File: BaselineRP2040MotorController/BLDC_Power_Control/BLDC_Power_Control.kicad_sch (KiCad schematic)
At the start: 7 parts, among them J3 Conn_01x03

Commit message: Change Mosfet Footprint.
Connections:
- net Motor Phase ${PhaseDesignator}/${PhaseDesignator}_OUT is gone; now on net Motor Phase ${PhaseDesignator}/${PhaseDesignator}_OUT: J3.3 (Pin_3)
- net Motor Phase ${PhaseDesignator}/${PhaseDesignator}_OUT: no longer J3.1 (Pin_1)
- new net Motor Phase ${PhaseDesignator}/${PhaseDesignator}_OUT: J3.1 (Pin_1)
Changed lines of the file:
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@@
 			(effects
 				(font
-					(size 0.001 0.001)
+					(size 0.0254 0.0254)
 				)
 				(hide yes)
@@
 			(effects
 				(font
-					(size 0.001 0.001)
+					(size 0.0254 0.0254)
 				)
 				(hide yes)
@@
 			(effects
 				(font
-					(size 0.001 0.001)
+					(size 0.0254 0.0254)
 				)
 				(hide yes)
@@
 			(effects
 				(font
-					(size 0.001 0.001)
+					(size 0.0254 0.0254)
 				)
 				(hide yes)
@@
 			(effects
 				(font
-					(size 0.001 0.001)
+					(size 0.0254 0.0254)
 				)
 				(hide yes)
@@
 			(effects
 				(font
-					(size 0.001 0.001)
+					(size 0.0254 0.0254)
 				)
 				(hide yes)
@@
 			(effects
 				(font
-					(size 0.001 0.001)
+					(size 0.0254 0.0254)
 				)
 				(hide yes)
@@
 			(effects
 				(font
-					(size 0.001 0.001)
+					(size 0.0254 0.0254)
 				)
 				(hide yes)
@@
 			(effects
 				(font
-					(size 0.001 0.001)
+					(size 0.0254 0.0254)
 				)
 				(hide yes)
@@
 			(effects
 				(font
-					(size 0.001 0.001)
-				)
-				(hide yes)
+					(size 0.0254 0.0254)
+				)
+				(hide yes)

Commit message: Drop some features.
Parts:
- C36, C37: footprint Capacitor_THT:CP_Radial_D10.0mm_P5.00mm -> Capacitor_SMD:CP_Elec_8x10
- J3: footprint parts:MT60-F.G.Y -> [EastMakes] Connectors:MT60-F.G.Y
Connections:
- net Motor Phase ${PhaseDesignator}/${PhaseDesignator}_OUT is gone; now on net Motor Phase ${PhaseDesignator}/${PhaseDesignator}_OUT: J3.3 (Pin_3)
- net Motor Phase ${PhaseDesignator}/${PhaseDesignator}_OUT: no longer J3.1 (Pin_1)
- new net Motor Phase ${PhaseDesignator}/${PhaseDesignator}_OUT: J3.1 (Pin_1)
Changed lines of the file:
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@@
 			)
 		)
-		(property "Footprint" "Capacitor_THT:CP_Radial_D10.0mm_P5.00mm"
+		(property "Footprint" "Capacitor_SMD:CP_Elec_8x10"
 			(at 249.8852 148.59 0)
 			(effects
@@
 			)
 		)
-		(property "Footprint" "Capacitor_THT:CP_Radial_D10.0mm_P5.00mm"
+		(property "Footprint" "Capacitor_SMD:CP_Elec_8x10"
 			(at 260.0452 148.59 0)
 			(effects
@@
 			)
 		)
-		(property "Footprint" "parts:MT60-F.G.Y"
+		(property "Footprint" "[EastMakes] Connectors:MT60-F.G.Y"
 			(at 170.18 74.93 0)
 			(effects

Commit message: Just before dropping the self build of the 2040
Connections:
- net Motor Phase ${PhaseDesignator}/${PhaseDesignator}_OUT is gone; now on net Motor Phase ${PhaseDesignator}/${PhaseDesignator}_OUT: J3.3 (Pin_3)
- net Motor Phase ${PhaseDesignator}/${PhaseDesignator}_OUT: no longer J3.1 (Pin_1)
- new net Motor Phase ${PhaseDesignator}/${PhaseDesignator}_OUT: J3.1 (Pin_1)
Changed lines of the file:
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@@
-	(wire
-		(pts
-			(xy 96.52 106.68) (xy 106.68 106.68)
-		)
-		(stroke
-			(width 0)
-			(type default)
-		)
-	)
 	(wire
 		(pts
@@
 		(fields_autoplaced yes)
 		(effects
-			(font
-				(size 1.27 1.27)
-				(bold yes)
-			)
-			(justify right)
-		)
-	)
-	(hierarchical_label "X_SENSE"
-		(shape output)
-		(at 96.52 106.68 180)
-		(fields_autoplaced yes)
-		(effects

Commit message: Release for Review
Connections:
- net Motor Phase ${PhaseDesignator}/${PhaseDesignator}_OUT is gone; now on net Motor Phase ${PhaseDesignator}/${PhaseDesignator}_OUT: J3.3 (Pin_3)
- net Motor Phase ${PhaseDesignator}/${PhaseDesignator}_OUT: no longer J3.1 (Pin_1)
- new net Motor Phase ${PhaseDesignator}/${PhaseDesignator}_OUT: J3.1 (Pin_1)
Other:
- moved on the sheet: C34, C35, C36, C37, C38, D14, J3

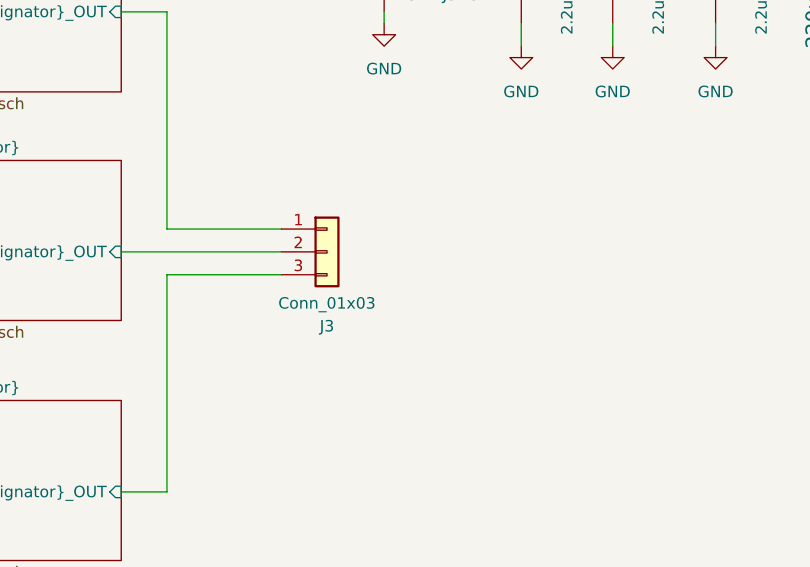
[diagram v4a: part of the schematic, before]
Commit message: Generate PDF
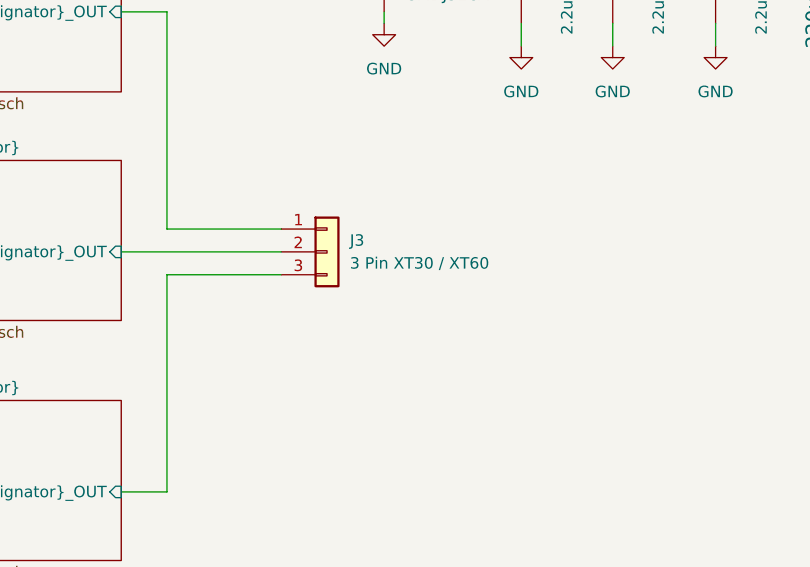
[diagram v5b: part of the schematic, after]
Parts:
- J3: value Conn_01x03 -> 3 Pin XT30 / XT60
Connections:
- net Motor Phase ${PhaseDesignator}/${PhaseDesignator}_OUT is gone; now on net Motor Phase ${PhaseDesignator}/${PhaseDesignator}_OUT: J3.3 (Pin_3)
- net Motor Phase ${PhaseDesignator}/${PhaseDesignator}_OUT: no longer J3.1 (Pin_1)
- new net Motor Phase ${PhaseDesignator}/${PhaseDesignator}_OUT: J3.1 (Pin_1)
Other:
- title: (none) -> BLDC Starting Point
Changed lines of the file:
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@@
 	(generator_version "8.0")
 	(paper "A5")
+	(title_block
+		(title "BLDC Starting Point")
+		(comment 1 "Florian, Josh and EMF Group Release")
+	)
 	(junction
 		(at 177.8 21.59)
@@
 		(fields_autoplaced yes)
 		(property "Reference" "J3"
-			(at 119.38 67.945 0)
-			(effects
-				(font
-					(size 1.27 1.27)
-				)
-			)
-		)
-		(property "Value" "Conn_01x03"
-			(at 119.38 65.405 0)
-			(effects
-				(font
-					(size 1.27 1.27)
-				)
-			)
-		)
+			(at 121.92 58.4199 0)
+			(effects
+				(font
+					(size 1.27 1.27)
+				)
+				(justify left)
+			)
+		)
+		(property "Value" "3 Pin XT30 / XT60"
+			(at 121.92 60.9599 0)
+			(effects
+				(font
+					(size 1.27 1.27)
+				)
+				(justify left)
+			)
+		)

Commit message: Post Feedback Changes.
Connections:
- net Motor Phase ${PhaseDesignator}/${PhaseDesignator}_OUT is gone; now on net Motor Phase ${PhaseDesignator}/${PhaseDesignator}_OUT: J3.3 (Pin_3)
- net Motor Phase ${PhaseDesignator}/${PhaseDesignator}_OUT: no longer J3.1 (Pin_1)
- net VMOT renamed VMOT_PWR
- new net Motor Phase ${PhaseDesignator}/${PhaseDesignator}_OUT: J3.1 (Pin_1)
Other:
- moved on the sheet: D14
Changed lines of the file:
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@@
-	)
-	(junction
-		(at 125.73 25.4)
-		(diameter 0)
-		(color 0 0 0 0)
 	)
 	(junction
@@
 	(wire
 		(pts
-			(xy 125.73 34.29) (xy 125.73 33.02)
-		)
-		(stroke
-			(width 0)
-			(type default)
-		)
-	)
-	(wire
-		(pts
-			(xy 125.73 24.13) (xy 125.73 25.4)
+			(xy 125.73 35.56) (xy 125.73 34.29)
+		)
+		(stroke
+			(width 0)
+			(type default)
+		)
+	)
+	(wire
+		(pts
+			(xy 125.73 24.13) (xy 125.73 26.67)
 		)
 		(stroke
@@
 		(pts
 			(xy 162.56 34.29) (xy 162.56 36.83)
-		)
-		(stroke
-			(width 0)
-			(type default)
-		)
-	)
-	(wire
-		(pts
-			(xy 124.46 25.4) (xy 125.73 25.4)
 		)
 		(stroke
@@
 		(shape output)
 		(at 45.72 91.44 180)
-		(fields_autoplaced yes)
-		(effects
-			(font
-				(size 1.27 1.27)
-				(bold yes)
-			)
-			(justify right)
-		)
-	)
-	(hierarchical_label "VMOT_PWR"
-		(shape input)
-		(at 124.46 25.4 180)
 		(fields_autoplaced yes)
 		(effects
@@
 		(on_board yes)
 		(dnp no)
-		(property "Reference" "#PWR074"
+		(property "Reference" "#PWR06"
 			(at 125.73 27.94 0)
 			(effects
@@
 			)
 		)
-		(property "Value" "VMOT"
+		(property "Value" "VMOT_PWR"
 			(at 125.73 20.32 0)
 			(effects
@@
 			(project "BaselineRP2040MotorController"
 				(path "/085e5f08-c826-4caa-b8e2-0a741609456e/adfc6ecc-6038-43a2-a2be-baacb83b86f1"
-					(reference "#PWR074")
+					(reference "#PWR06")
 					(unit 1)
 				)
@@
 	(symbol
 		(lib_id "power:GND")
-		(at 125.73 34.29 0)
+		(at 125.73 35.56 0)
 		(unit 1)
 		(exclude_from_sim no)
@@
 		(fields_autoplaced yes)
 		(property "Reference" "#PWR075"
+			(at 125.73 41.91 0)
+			(effects
+				(font
+					(size 1.27 1.27)
+				)
+				(hide yes)
+			)
+		)
+		(property "Value" "GND"
 			(at 125.73 40.64 0)
 			(effects
@@
 					(size 1.27 1.27)
 				)
-				(hide yes)
-			)
-		)
-		(property "Value" "GND"
-			(at 125.73 39.37 0)
-			(effects
-				(font
-					(size 1.27 1.27)
-				)
 			)
 		)
 		(property "Footprint" ""
-			(at 125.73 34.29 0)
+			(at 125.73 35.56 0)
 			(effects
 				(font
@@
 		)
 		(property "Datasheet" ""
-			(at 125.73 34.29 0)
+			(at 125.73 35.56 0)
 			(effects
 				(font
@@
 		)
 		(property "Description" "Power symbol creates a global label with name \"GND\" , ground"
-			(at 125.73 34.29 0)
+			(at 125.73 35.56 0)
 			(effects
 				(font
@@
 	(symbol
 		(lib_id "Diode:SMF54A")
-		(at 125.73 29.21 270)
+		(at 125.73 30.48 270)
 		(unit 1)
 		(exclude_from_sim no)
@@
 		(fields_autoplaced yes)
 		(property "Reference" "D14"
-			(at 128.27 28.575 90)
+			(at 128.27 29.845 90)
 			(effects
 				(font
@@
 		)
 		(property "Value" "SMDJ51CA"
-			(at 128.27 31.115 90)
+			(at 128.27 32.385 90)
 			(effects
 				(font
@@
 		)
 		(property "Footprint" "Diode_SMD:D_SMF"
-			(at 120.65 29.21 0)
+			(at 120.65 30.48 0)
 			(effects
 				(font
@@
 		)
 		(property "Datasheet" "https://www.vishay.com/doc?85881"
-			(at 125.73 27.94 0)
+			(at 125.73 29.21 0)
 			(effects
 				(font
@@
 		)
 		(property "Description" "200W unidirectional Transil Transient Voltage Suppressor, 54Vrwm, SMF"
-			(at 125.73 29.21 0)
+			(at 125.73 30.48 0)
 			(effects
 				(font
@@
 		)
 		(property "LCSC" "C406702"
-			(at 125.73 29.21 90)
+			(at 125.73 30.48 90)
 			(effects
 				(font
@@
 			)
 		)
-		(property "Value" "VMOT"
+		(property "Value" "VMOT_PWR"
 			(at 140.97 20.32 0)
 			(effects
@@
 			)
 		)
-		(property "Value" "VMOT"
+		(property "Value" "VMOT_PWR"
 			(at 162.56 20.32 0)
 			(effects
@@
 			)
 		)
-		(property "Value" "VMOT"
+		(property "Value" "VMOT_PWR"
 			(at 151.13 20.32 0)
 			(effects
@@
 			)
 		)
-		(property "Value" "VMOT"
+		(property "Value" "VMOT_PWR"
 			(at 177.8 17.145 0)
 			(effects

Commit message: Make BOM
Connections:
- net Motor Phase ${PhaseDesignator}/${PhaseDesignator}_OUT is gone; now on net Motor Phase ${PhaseDesignator}/${PhaseDesignator}_OUT: J3.3 (Pin_3)
- net Motor Phase ${PhaseDesignator}/${PhaseDesignator}_OUT: no longer J3.1 (Pin_1)
- new net Motor Phase ${PhaseDesignator}/${PhaseDesignator}_OUT: J3.1 (Pin_1)
